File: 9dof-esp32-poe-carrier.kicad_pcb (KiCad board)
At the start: 2 copper layers, 31 x 50 mm, 6 parts, among them J1 Input Power, J2 Stemma QT, J3 UEXT_Slave, J4 WS2811_strand, J5 USB_A, U1 AMS1117-5.0

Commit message: Updated redone schematic.
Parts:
- removed J1: Input Power, Connector_BarrelJack:BarrelJack_Horizontal
- removed J2: Stemma QT, Connector_JST:JST_SH_SM04B-SRSS-TB_1x04-1MP_P1.00mm_Horizontal
- removed J3: UEXT_Slave, Connector_PinHeader_2.54mm:PinHeader_2x05_P2.54mm_Vertical
- removed J4: WS2811_strand, Connector_PinHeader_2.54mm:PinHeader_1x03_P2.54mm_Vertical
- removed J5: USB_A, Connector_USB:USB_A_Receptacle_GCT_USB1046
- removed U1: AMS1117-5.0, Package_TO_SOT_SMD:SOT-223-3_TabPin2
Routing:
- net 0: track 0.00 -> 218.3 mm
- net +12V: track 38.5 -> 0.00 mm
- net DO: track 27.9 -> 0.00 mm
- net +3V3: track 18.2 -> 0.00 mm
- net SDA: track 16.1 -> 0.00 mm, vias 1 -> 0
- net SCL: track 12.0 -> 0.00 mm
- net +5V: track 10.2 -> 0.00 mm
- net (no net): vias 0 -> 24
- removed copper zone on F.Cu, net GND
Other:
- board size 31 x 50 mm -> 25.4 x 99.1 mm

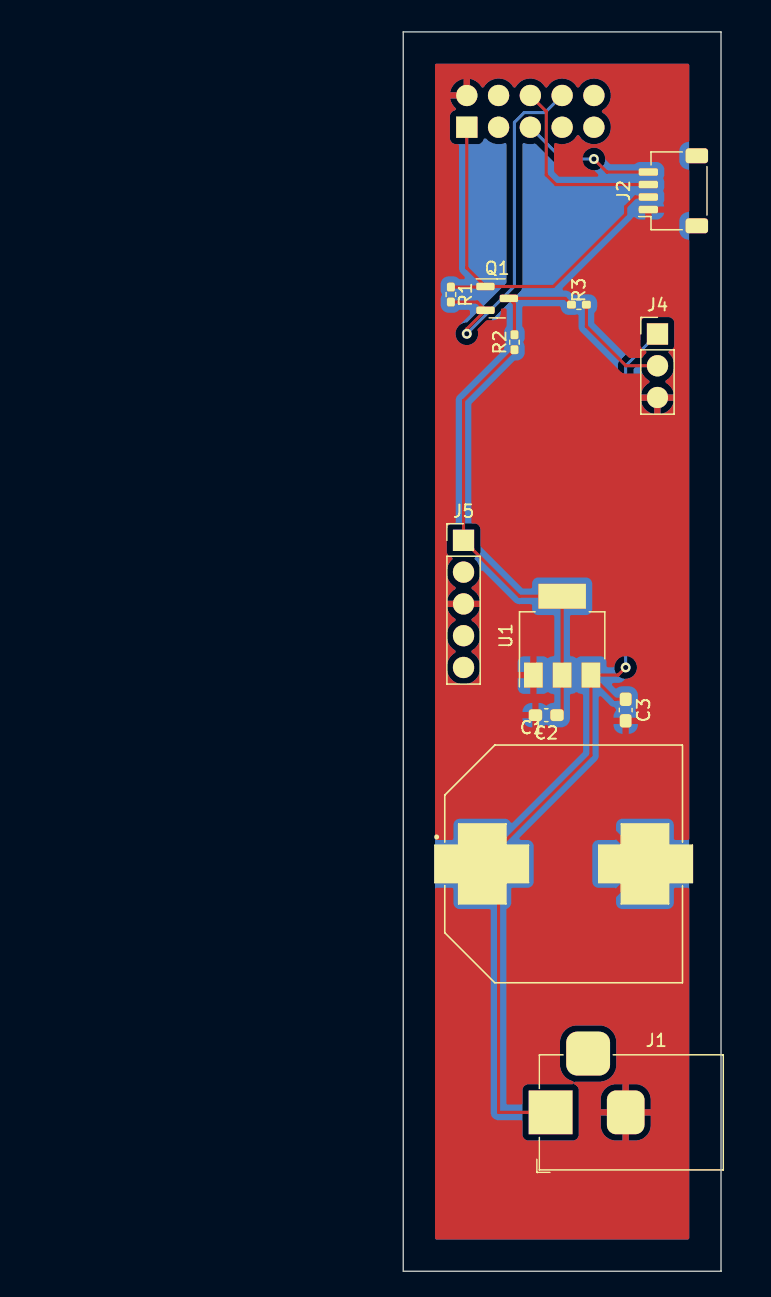
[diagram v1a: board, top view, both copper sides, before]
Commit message: Fiddle with parts, add via stiching, add silkscreen labels.
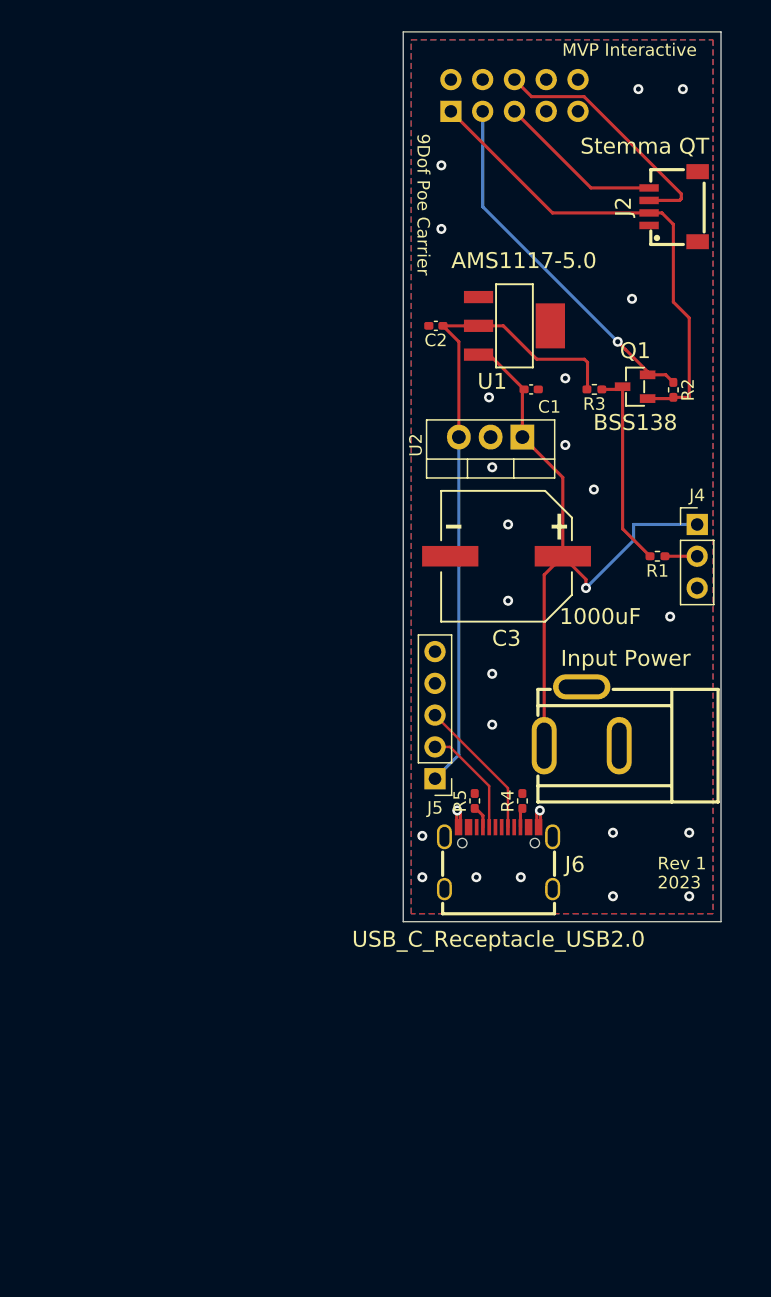
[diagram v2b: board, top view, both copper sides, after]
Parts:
- added C1: 10uF, Capacitor_SMD:C_0402_1005Metric_Pad0.74x0.62mm_HandSolder, F.Cu at (116.9, 92.1)
- added C2: 10uF, Capacitor_SMD:C_0402_1005Metric_Pad0.74x0.62mm_HandSolder, F.Cu at (109.3, 87.0)
- added C3: 1000uF, EasyEDA_Footprints:CAP-SMD_BD10.0-L10.3-W10.3-FD, F.Cu at (114.9, 105.4)
- added J1: Input Power, EasyEDA_Footprints:DC-IN-TH_DC005-T, F.Cu at (120.9, 118.2)
- added J2: Stemma QT, EasyEDA_Footprints:CONN-SMD_4P-P1.00_SM04B-SRSS-TB-LF-SN, F.Cu at (128.3, 77.5)
- added J3: UEXT_Slave, Library:UEXT_SLAVE_BACKSIDE, B.Cu at (118.1, 62.2)
- added J4: WS2811_strand, Connector_PinHeader_2.54mm:PinHeader_1x03_P2.54mm_Vertical, F.Cu at (130.2, 102.9)
- added J5: USB to ESP32, Connector_PinHeader_2.54mm:PinHeader_1x05_P2.54mm_Vertical, F.Cu at (109.2, 123.2)
- added J6: USB_C_Receptacle_USB2.0, EasyEDA_Footprints:USB-C_SMD-TYPE-C-31-M-12, F.Cu at (114.3, 129.5)
- added Q1: BSS138, EasyEDA_Footprints:SOT-23-3_L2.9-W1.3-P1.90-LS2.4-BR, F.Cu at (125.2, 91.9)
- added R1: 470, Resistor_SMD:R_0402_1005Metric_Pad0.72x0.64mm_HandSolder, F.Cu at (127.0, 105.4)
- added R2: 10K, Resistor_SMD:R_0402_1005Metric_Pad0.72x0.64mm_HandSolder, F.Cu at (128.3, 92.1)
- added R3: 10K, Resistor_SMD:R_0402_1005Metric_Pad0.72x0.64mm_HandSolder, F.Cu at (122.0, 92.1)
- added R4: 5.1k, Resistor_SMD:R_0402_1005Metric_Pad0.72x0.64mm_HandSolder, F.Cu at (116.2, 125.0)
- added R5: 5.1k, Resistor_SMD:R_0402_1005Metric_Pad0.72x0.64mm_HandSolder, F.Cu at (112.4, 125.0)
- added U1: AMS1117-5.0, EasyEDA_Footprints:SOT-223-3_L6.7-W3.7-P2.30-LS7.0-BR, F.Cu at (115.6, 87.0)
- added U2: STM L7805CV, Package_TO_SOT_THT:TO-220-3_Vertical, F.Cu at (116.2, 95.9)
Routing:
- net 0: track 218.3 -> 0.00 mm
- net +5V: track 0.00 -> 52.5 mm
- net +12V: track 0.00 -> 50.3 mm, vias 0 -> 1
- net +3V3: track 0.00 -> 39.2 mm
- net DO3v3: track 0.00 -> 28.8 mm, vias 0 -> 1
- net SDA: track 0.00 -> 20.1 mm
- net DINv5: track 0.00 -> 16.2 mm
- net SCL: track 0.00 -> 13.3 mm
- net D+: track 0.00 -> 11.4 mm
- net D-: track 0.00 -> 8.91 mm
- net GND: track 0.00 -> 5.59 mm, vias 0 -> 25
- net Net-(J4-Pin_2): track 0.00 -> 2.58 mm
- net Net-(J6-CC1): track 0.00 -> 1.86 mm
- net Net-(J6-CC2): track 0.00 -> 1.65 mm
- net (no net): vias 24 -> 0
- added copper zone on B.Cu, net GND
- added copper zone on F.Cu, net GND
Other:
- board size 25.4 x 99.1 mm -> 25.4 x 71.1 mm
- board text added: "2023"
- board text added: "9Dof Poe Carrier"
- board text added: "MVP Interactive"
- board text added: "Rev 1"
